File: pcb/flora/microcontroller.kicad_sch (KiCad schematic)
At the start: 17 parts, among them IC1 ESP32-WROOM-32E(8MB), J7 Conn_01x20, J8 Conn_01x04, J9 Conn_01x20, Q1 MUN5214DW1T1G

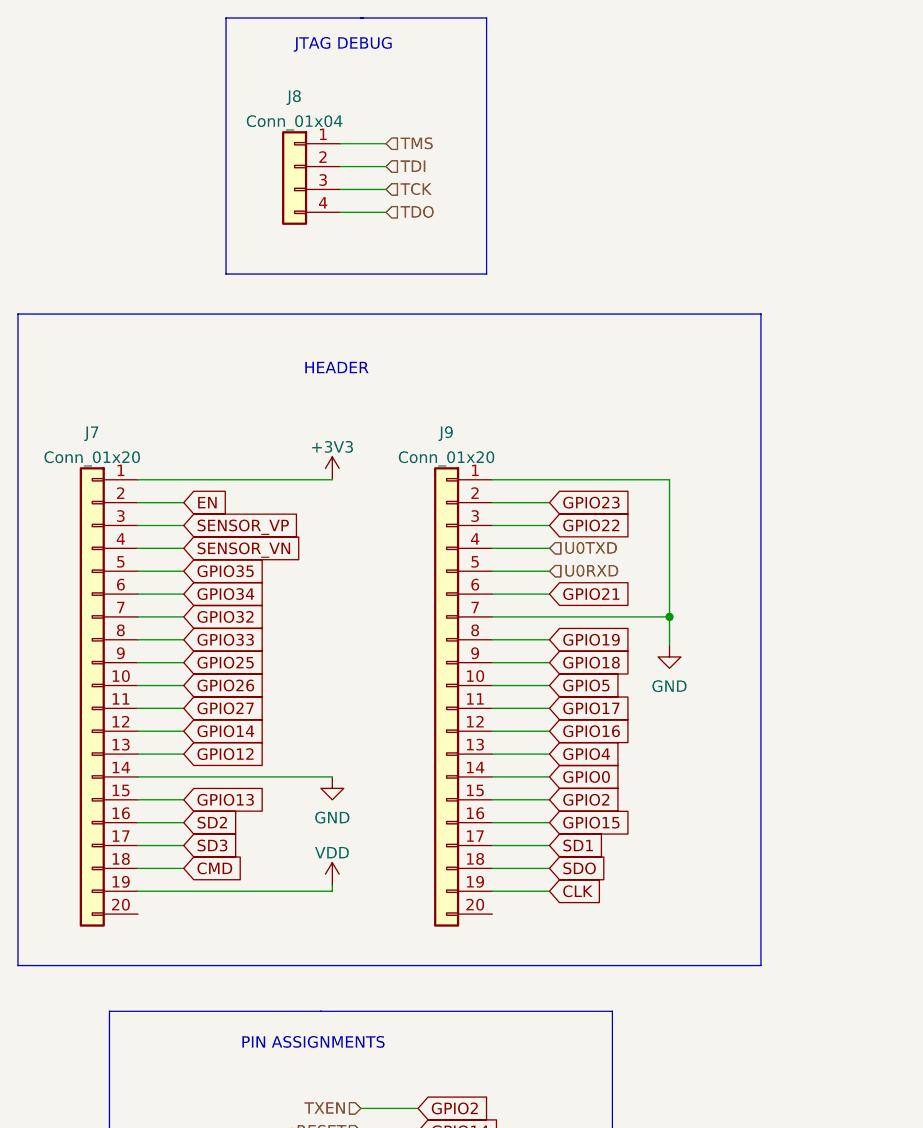
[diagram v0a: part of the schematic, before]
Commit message: Removed header
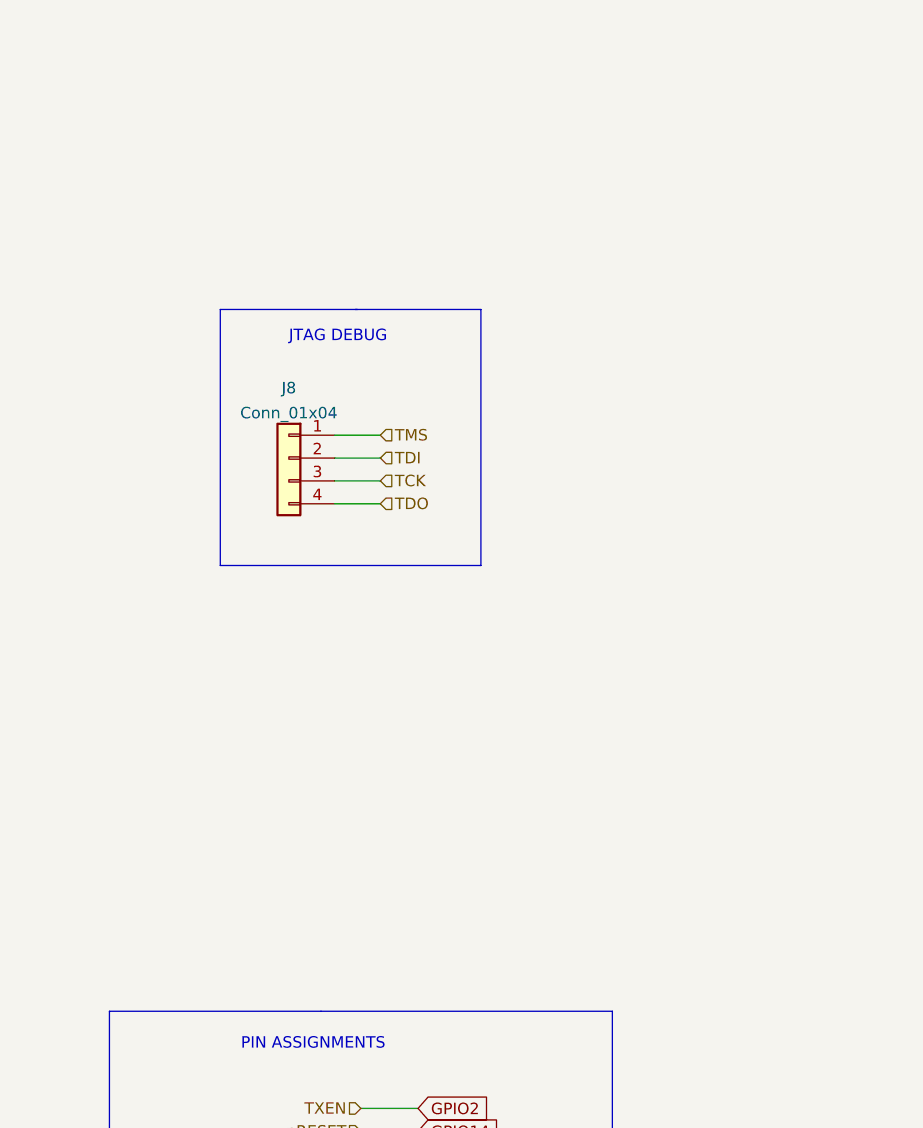
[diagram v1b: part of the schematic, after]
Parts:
- removed J7, J9: Conn_01x20, Connector_PinHeader_1.00mm:PinHeader_1x20_P1.00mm_Vertical, symbol Connector_Generic:Conn_01x20
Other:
- note removed: "HEADER"
- moved on the sheet: J8

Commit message: released Rev A
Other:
- note added: "TOUCH4"
- note added: "TOUCH5"
- note added: "TOUCH6"
- title: (none) -> FLORA
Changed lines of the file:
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@@
 (kicad_sch (version 20211123) (generator eeschema)
   (paper "A3")
+  (title_block
+    (title "FLORA")
+    (date "2022-04-27")
+    (rev "A")
+  )
   (junction (at 350.393 94.615) (diameter 0) (color 0 0 0 0)
   )
@@
     (effects (font (size 1.27 1.27)) (justify left bottom))
   )
+  (text "TOUCH6" (at 101.6 213.36 0)
+    (effects (font (size 1.27 1.27)) (justify left bottom))
+  )
   (text "JTAG DEBUG" (at 75.819 73.787 0)
     (effects (font (size 1.27 1.27)) (justify left bottom))
   )
+  (text "TOUCH4" (at 101.6 218.44 0)
+    (effects (font (size 1.27 1.27)) (justify left bottom))
+  )
   (text "I2C" (at 65.405 207.01 0)
+    (effects (font (size 1.27 1.27)) (justify left bottom))
+  )
+  (text "TOUCH5" (at 101.6 215.9 0)
     (effects (font (size 1.27 1.27)) (justify left bottom))
   )
@@
     )
   )
-  (global_label "GPIO33" (shape input) (at 90.17 217.17 0) (fields_autoplaced)
-    (effects (font (size 1.27 1.27)) (justify left))
-    (property "Intersheet References" "${INTERSHEET_REFS}" (id 0) (at 99.4774 217.0906 0)
-      (effects (font (size 1.27 1.27)) (justify left) hide)
-    )
-  )
   (global_label "GPIO35" (shape input) (at 273.05 179.705 0) (fields_autoplaced)
     (effects (font (size 1.27 1.27)) (justify left))
@@
     )
   )
-  (global_label "GPIO35" (shape input) (at 90.17 214.63 0) (fields_autoplaced)
-    (effects (font (size 1.27 1.27)) (justify left))
-    (property "Intersheet References" "${INTERSHEET_REFS}" (id 0) (at 99.4774 214.5506 0)
+  (global_label "GPIO13" (shape input) (at 90.17 217.17 0) (fields_autoplaced)
+    (effects (font (size 1.27 1.27)) (justify left))
+    (property "Intersheet References" "${INTERSHEET_REFS}" (id 0) (at 99.4774 217.0906 0)
       (effects (font (size 1.27 1.27)) (justify left) hide)
     )
@@
     )
   )
+  (global_label "GPIO12" (shape input) (at 90.17 214.63 0) (fields_autoplaced)
+    (effects (font (size 1.27 1.27)) (justify left))
+    (property "Intersheet References" "${INTERSHEET_REFS}" (id 0) (at 99.4774 214.5506 0)
+      (effects (font (size 1.27 1.27)) (justify left) hide)
+    )
+  )
   (global_label "GPIO5" (shape input) (at 273.05 133.985 0) (fields_autoplaced)
     (effects (font (size 1.27 1.27)) (justify left))
@@
     )
   )
+  (global_label "GPIO14" (shape input) (at 90.17 212.09 0) (fields_autoplaced)
+    (effects (font (size 1.27 1.27)) (justify left))
+    (property "Intersheet References" "${INTERSHEET_REFS}" (id 0) (at 99.4774 212.0106 0)
+      (effects (font (size 1.27 1.27)) (justify left) hide)
+    )
+  )
   (global_label "SD2" (shape input) (at 205.74 146.685 180) (fields_autoplaced)
     (effects (font (size 1.27 1.27)) (justify right))
@@
       (effects (font (size 1.27 1.27)) (justify left) hide)
     )
-  )
-  (global_label "GPIO34" (shape input) (at 90.17 212.09 0) (fields_autoplaced)
-    (effects (font (size 1.27 1.27)) (justify left))
-    (property "Intersheet References" "${INTERSHEET_REFS}" (id 0) (at 99.4774 212.0106 0)
-      (effects (font (size 1.27 1.27)) (justify left) hide)
-    )

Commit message: added image
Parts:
- removed J8: Conn_01x04, Connector_PinHeader_1.27mm:PinHeader_1x04_P1.27mm_Vertical, symbol Connector_Generic:Conn_01x04
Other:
- note removed: "JTAG DEBUG"
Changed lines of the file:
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@@
   (title_block
     (title "FLORA")
-    (date "2022-04-27")
-    (rev "A")
+    (date "2022-06-01")
+    (rev "B")
   )
   (junction (at 350.393 94.615) (diameter 0) (color 0 0 0 0)
@@
   (junction (at 222.885 111.125) (diameter 0) (color 0 0 0 0)
   )
-  (wire (pts (xy 80.899 89.027) (xy 85.979 89.027))
-    (stroke (width 0) (type default) (color 0 0 0 0))
-  )
   (wire (pts (xy 212.09 97.79) (xy 212.09 100.33))
     (stroke (width 0) (type default) (color 0 0 0 0))
@@
     (stroke (width 0) (type default) (color 0 0 0 0))
   )
-  (polyline (pts (xy 97.155 98.425) (xy 68.199 98.425))
-    (stroke (width 0) (type default) (color 0 0 0 0))
-  )
   (wire (pts (xy 240.665 191.77) (xy 243.205 191.77))
     (stroke (width 0) (type default) (color 0 0 0 0))
@@
     (stroke (width 0) (type default) (color 0 0 0 0))
   )
-  (polyline (pts (xy 83.185 69.977) (xy 97.155 69.977))
-    (stroke (width 0) (type default) (color 0 0 0 0))
-  )
   (wire (pts (xy 347.853 107.315) (xy 324.358 107.315))
     (stroke (width 0) (type default) (color 0 0 0 0))
@@
     (stroke (width 0) (type default) (color 0 0 0 0))
   )
-  (wire (pts (xy 80.899 86.487) (xy 85.979 86.487))
-    (stroke (width 0) (type default) (color 0 0 0 0))
-  )
   (wire (pts (xy 273.05 136.525) (xy 268.605 136.525))
     (stroke (width 0) (type default) (color 0 0 0 0))
@@
     (stroke (width 0) (type default) (color 0 0 0 0))
   )
-  (wire (pts (xy 80.899 91.567) (xy 85.979 91.567))
-    (stroke (width 0) (type default) (color 0 0 0 0))
-  )
-  (wire (pts (xy 80.899 83.947) (xy 85.979 83.947))
-    (stroke (width 0) (type default) (color 0 0 0 0))
-  )
   (wire (pts (xy 321.183 130.175) (xy 321.183 118.11))
     (stroke (width 0) (type default) (color 0 0 0 0))
@@
     (stroke (width 0) (type default) (color 0 0 0 0))
   )
-  (polyline (pts (xy 68.199 98.425) (xy 68.199 69.977))
-    (stroke (width 0) (type default) (color 0 0 0 0))
-  )
   (wire (pts (xy 212.09 111.125) (xy 212.09 107.95))
     (stroke (width 0) (type default) (color 0 0 0 0))
@@
     (stroke (width 0) (type default) (color 0 0 0 0))
   )
-  (polyline (pts (xy 97.155 69.977) (xy 97.155 98.425))
-    (stroke (width 0) (type default) (color 0 0 0 0))
-  )
   (wire (pts (xy 204.47 128.905) (xy 204.47 111.125))
     (stroke (width 0) (type default) (color 0 0 0 0))
@@
   )
   (wire (pts (xy 350.393 94.615) (xy 361.188 94.615))
-    (stroke (width 0) (type default) (color 0 0 0 0))
-  )
-  (polyline (pts (xy 68.199 69.977) (xy 83.439 69.977))
     (stroke (width 0) (type default) (color 0 0 0 0))
   )
@@
     (effects (font (size 1.27 1.27)) (justify left bottom))
   )
-  (text "JTAG DEBUG" (at 75.819 73.787 0)
-    (effects (font (size 1.27 1.27)) (justify left bottom))
-  )
   (text "TOUCH4" (at 101.6 218.44 0)
     (effects (font (size 1.27 1.27)) (justify left bottom))
@@
     (effects (font (size 1.27 1.27)) (justify right))
   )
-  (hierarchical_label "TDO" (shape input) (at 85.979 91.567 0)
-    (effects (font (size 1.27 1.27)) (justify left))
-  )
   (hierarchical_label "RXEN" (shape input) (at 83.82 179.07 180)
     (effects (font (size 1.27 1.27)) (justify right))
@@
     (effects (font (size 1.27 1.27)) (justify right))
   )
-  (hierarchical_label "TMS" (shape input) (at 85.979 83.947 0)
-    (effects (font (size 1.27 1.27)) (justify left))
-  )
   (hierarchical_label "DIO3" (shape input) (at 83.82 186.69 180)
     (effects (font (size 1.27 1.27)) (justify right))
@@
     (effects (font (size 1.27 1.27)) (justify right))
   )
-  (hierarchical_label "TCK" (shape input) (at 85.979 89.027 0)
-    (effects (font (size 1.27 1.27)) (justify left))
-  )
   (hierarchical_label "SOIL_3" (shape input) (at 83.82 217.17 180)
     (effects (font (size 1.27 1.27)) (justify right))
@@
   (hierarchical_label "TDI" (shape input) (at 83.82 191.77 180)
     (effects (font (size 1.27 1.27)) (justify right))
-  )
-  (hierarchical_label "TDI" (shape input) (at 85.979 86.487 0)
-    (effects (font (size 1.27 1.27)) (justify left))
   )
   (hierarchical_label "TMS" (shape input) (at 83.82 196.85 180)
@@
     (pin "1")
   )
-  (symbol (lib_id "Connector_Generic:Conn_01x04") (at 75.819 86.487 0) (mirror y) (unit 1)
-    (in_bom yes) (on_board yes) (fields_autoplaced)
-    (property "Reference" "J8" (id 0) (at 75.819 78.7105 0))
-    (property "Value" "Conn_01x04" (id 1) (at 75.819 81.4856 0))
-    (property "Footprint" "Connector_PinHeader_1.27mm:PinHeader_1x04_P1.27mm_Vertical" (id 2) (at 75.819 86.487 0)
-      (effects (font (size 1.27 1.27)) hide)
-    )
-    (property "Datasheet" "~" (id 3) (at 75.819 86.487 0)
-      (effects (font (size 1.27 1.27)) hide)
-    )
-    (pin "1")
-    (pin "2")
-    (pin "3")
-    (pin "4")
-  )
 )

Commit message: commit backups
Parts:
- C16: LCSC C45783 -> C602037
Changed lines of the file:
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@@
       (effects (font (size 1.27 1.27)) (justify left))
     )
-    (property "LCSC" "C45783" (id 5) (at 212.09 104.14 0)
+    (property "LCSC" "C602037" (id 5) (at 212.09 104.14 0)
       (effects (font (size 1.27 1.27)) hide)
     )
